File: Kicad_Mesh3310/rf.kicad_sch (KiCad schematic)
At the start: 34 parts, among them U1 TPE4259-63, U10 SX1262IMLTRT, X1 S201632M10PF10PPM 32MHz

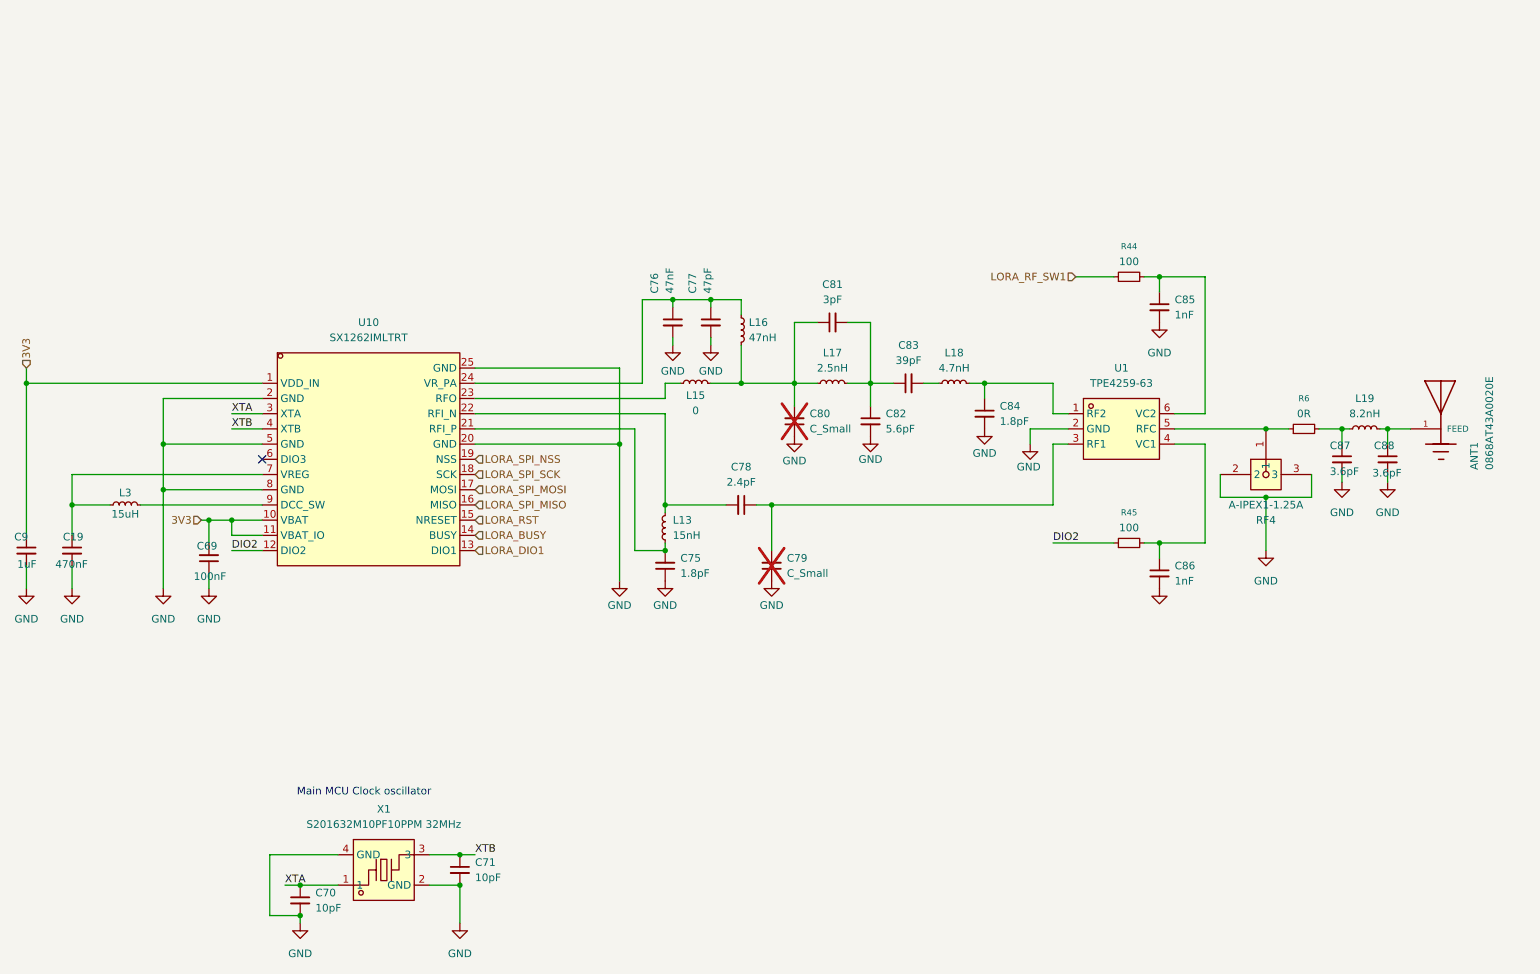
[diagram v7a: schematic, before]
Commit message: Lora antenna replacement
Lora antenna replacement, added Nordic nRF 9151 for GPS , VoIP ,VoLTE-m , SIP
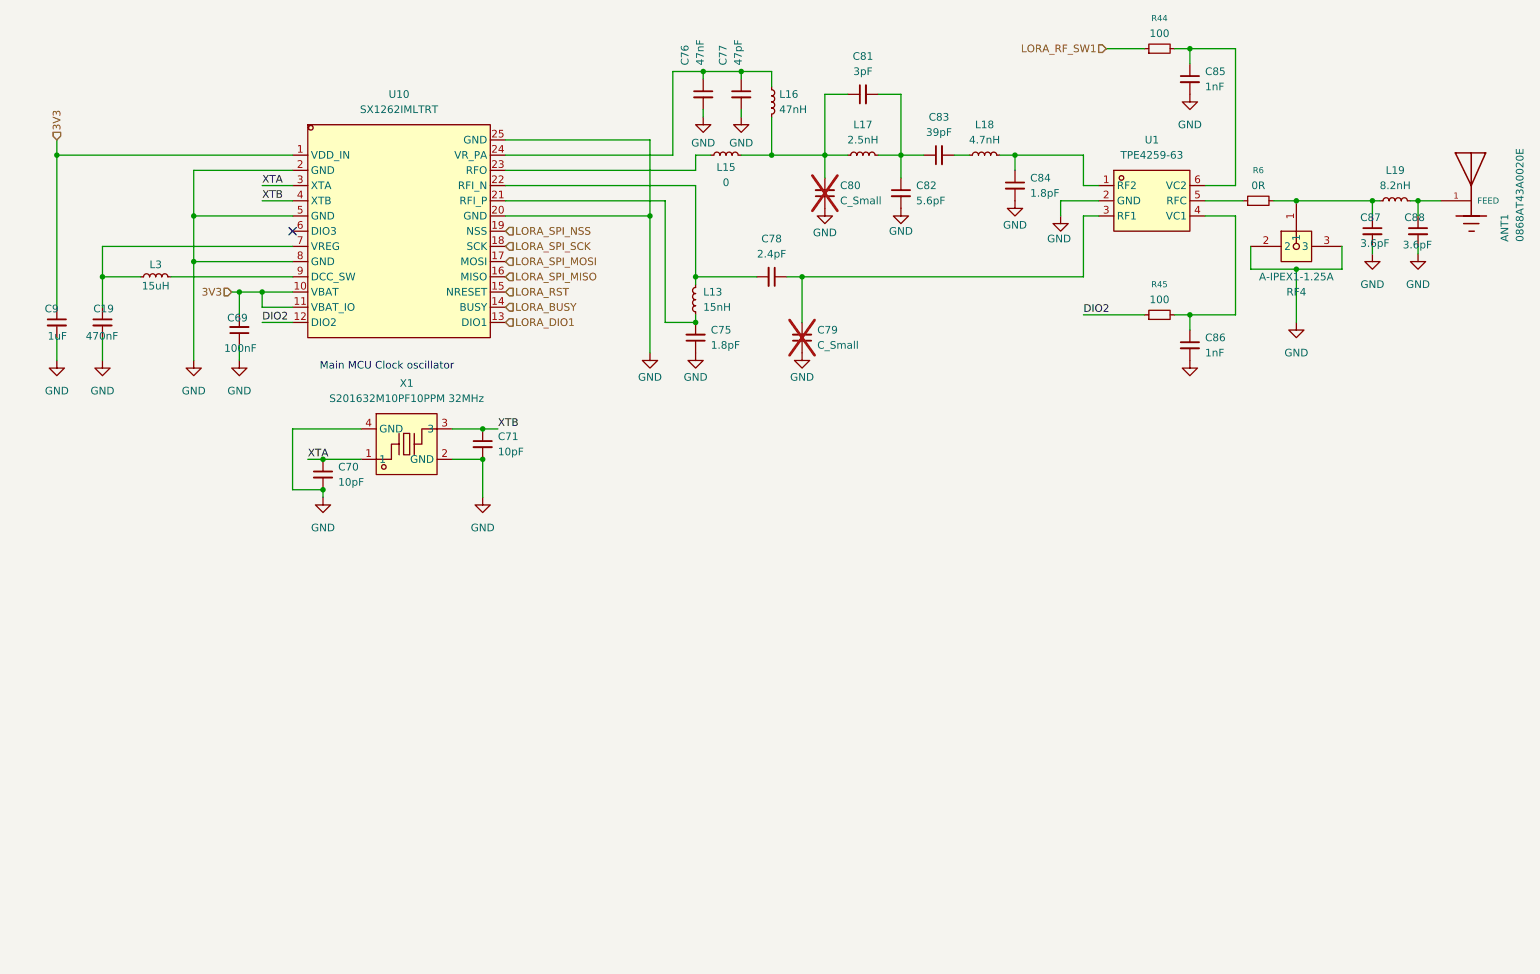
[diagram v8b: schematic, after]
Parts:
- C69, C70, C71, C75, C76, C77, C78, C79, C80, C81, C82, C83, C84, C85, C86, C87, C88: footprint Capacitor_SMD:C_0402_1005Metric -> Capacitor_SMD:C_0201_0603Metric
- L13, L15, L16, L17, L18, L19: footprint Inductor_SMD:L_0402_1005Metric -> Inductor_SMD:L_0201_0603Metric
- L3: footprint Inductor_SMD:L_0603_1608Metric -> Inductor_SMD:L_0201_0603Metric
- R44, R45, R6: footprint Resistor_SMD:R_0402_1005Metric -> Resistor_SMD:R_0201_0603Metric
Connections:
- net at R6.1, U1.5 (RFC): no longer RF4.1
- net at C87.1, L19.1, R6.2: now also RF4.1
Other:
- moved on the sheet: ANT1, C19, C69, C70, C71, C75, C76, C77, C78, C79, C80, C81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
